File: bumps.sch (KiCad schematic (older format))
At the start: 136 parts, among them M1 CONN_1, M2 CONN_1, M3 CONN_1, P1 DIL6, P10 Mot-A, P11 Mot-A, P12 Mot-X, P13 T1, P14 T2, P15 T3, P16 MPower, P17 PWM-2, P18 PWM-1, P19 END-X, P2 DIL6, P20 END-Y, P21 END-Z, P22 Mot-X, P23 Mot-Y, P24 Mot-Y, P25 Mot-Z, P26 Mot-Z, P27 Aux, P29 PWM, P3 Mot-E, P4 Mot-E, P5 DIL6, P6 DIL6, P7 DIL6, P8 P8 Header, P9 P9 Header, Q1 IRLB8743PBF, Q2 IRLB8743PBF, Q3 FDS9926A, Q4 FDS9926A, U1 E-Polo, U2 A-Polo, U3 X-Polo, U4 Y-Polo, U5 Z-Polo, U6 MC34063, U7 AP1117/3.3

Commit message: o Fix components, that disappeared in the kicad library   (CONN_1, CONN_2 and CONN_4 don't exist anymore,   they are now CONN_01X01, CONN_01X02 and CONN_01x04). o Connect the new components that inconveniently have a different   shape, so don't connect to the original pins anymore. o My statement regarding this non-backward compatible library   change: "&%@3$%*!@"  :)
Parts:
- M1, M2, M3: symbol CONN_1 -> CONN_01X01
- P10, P11, P12, P22, P23, P24, P25, P26, P3, P4: symbol CONN_4 -> CONN_01X04
- P13, P14, P15, P16, P17, P18, P19, P20, P21, P27, P29: symbol CONN_2 -> CONN_01X02
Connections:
- wire segments 237 -> 263

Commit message: o Get rid of 100k pull-down for MS1. Not needed   (fixes #9)
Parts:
- removed R1, R2, R3, R4, R5: 100k, SMD_Packages:SM0805, symbol R
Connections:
- wire segments 263 -> 258
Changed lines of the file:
@@
 LIBS:valves
 LIBS:BUMPS
-LIBS:bumps-cache
 EELAYER 25 0
 EELAYER END
@@
 ~EN
 $Comp
-L R R1
-U 1 1 52EDAB15
-P 3700 4650
-F 0 "R1" V 3780 4650 40  0000 C CNN
-F 1 "100k" V 3707 4651 40  0000 C CNN
-F 2 "SMD_Packages:SM0805" V 3630 4650 30  0001 C CNN
-F 3 "" H 3700 4650 60  0001 C CNN
-	1    3700 4650
-	-1   0    0    1
-$EndComp
-$Comp
-L GND #PWR07
-U 1 1 52EDABD4
-P 3700 4900
-F 0 "#PWR07" H 3700 4900 30  0001 C CNN
-F 1 "GND" H 3700 4830 30  0001 C CNN
-F 2 "" H 3700 4900 60  0001 C CNN
-F 3 "" H 3700 4900 60  0001 C CNN
-	1    3700 4900
-	1    0    0    -1
-$EndComp
-$Comp
 L POLOLUSTEPPER U5
 U 1 1 52EDACE9
@@
 VDD_3V3
 $Comp
-L R R5
-U 1 1 52EDAD11
-P 7850 5050
-F 0 "R5" V 7930 5050 40  0000 C CNN
-F 1 "100k" V 7857 5051 40  0000 C CNN
-F 2 "SMD_Packages:SM0805" V 7780 5050 30  0001 C CNN
-F 3 "" H 7850 5050 60  0001 C CNN
-	1    7850 5050
-	-1   0    0    1
-$EndComp
-$Comp
-L GND #PWR010
-U 1 1 52EDAD22
-P 7850 5300
-F 0 "#PWR010" H 7850 5300 30  0001 C CNN
-F 1 "GND" H 7850 5230 30  0001 C CNN
-F 2 "" H 7850 5300 60  0001 C CNN
-F 3 "" H 7850 5300 60  0001 C CNN
-	1    7850 5300
-	-1   0    0    -1
-$EndComp
-$Comp
 L POLOLUSTEPPER U3
 U 1 1 52EDAD28
@@
 VDD_3V3
 $Comp
-L R R3
-U 1 1 52EDAD50
-P 7850 1750
-F 0 "R3" V 7930 1750 40  0000 C CNN
-F 1 "100k" V 7857 1751 40  0000 C CNN
-F 2 "SMD_Packages:SM0805" V 7780 1750 30  0001 C CNN
-F 3 "" H 7850 1750 60  0001 C CNN
-	1    7850 1750
-	-1   0    0    1
-$EndComp
-$Comp
-L GND #PWR013
-U 1 1 52EDAD61
-P 7850 2000
-F 0 "#PWR013" H 7850 2000 30  0001 C CNN
-F 1 "GND" H 7850 1930 30  0001 C CNN
-F 2 "" H 7850 2000 60  0001 C CNN
-F 3 "" H 7850 2000 60  0001 C CNN
-	1    7850 2000
-	1    0    0    -1
-$EndComp
-$Comp
 L POLOLUSTEPPER U4
 U 1 1 52EDAD67
@@
 VDD_3V3
 $Comp
-L R R4
-U 1 1 52EDAD8F
-P 7850 3400
-F 0 "R4" V 7930 3400 40  0000 C CNN
-F 1 "100k" V 7857 3401 40  0000 C CNN
-F 2 "SMD_Packages:SM0805" V 7780 3400 30  0001 C CNN
-F 3 "" H 7850 3400 60  0001 C CNN
-	1    7850 3400
-	-1   0    0    1
-$EndComp
-$Comp
-L GND #PWR016
-U 1 1 52EDADA0
-P 7850 3650
-F 0 "#PWR016" H 7850 3650 30  0001 C CNN
-F 1 "GND" H 7850 3580 30  0001 C CNN
-F 2 "" H 7850 3650 60  0001 C CNN
-F 3 "" H 7850 3650 60  0001 C CNN
-	1    7850 3650
-	1    0    0    -1
-$EndComp
-$Comp
 L POLOLUSTEPPER U2
 U 1 1 52EDADA6
@@
 Text GLabel 3100 5600 1    50   Input ~ 0
 VDD_3V3
-$Comp
-L R R2
-U 1 1 52EDADCE
-P 3700 6400
-F 0 "R2" V 3780 6400 40  0000 C CNN
-F 1 "100k" V 3707 6401 40  0000 C CNN
-F 2 "SMD_Packages:SM0805" V 3630 6400 30  0001 C CNN
-F 3 "" H 3700 6400 60  0001 C CNN
-	1    3700 6400
-	-1   0    0    1
-$EndComp
-$Comp
-L GND #PWR019
-U 1 1 52EDADDF
-P 3700 6650
-F 0 "#PWR019" H 3700 6650 30  0001 C CNN
-F 1 "GND" H 3700 6580 30  0001 C CNN
-F 2 "" H 3700 6650 60  0001 C CNN
-F 3 "" H 3700 6650 60  0001 C CNN
-	1    3700 6650
-	1    0    0    -1
-$EndComp
 Text GLabel 4100 1750 2    50   Output ~ 0
 STEP_X
@@
 	3900 4250 4300 4250
 Wire Wire Line
-	3700 4400 4050 4050
-Connection ~ 4050 4050
-Wire Wire Line
 	9950 5050 9950 5100
 Wire Wire Line
@@
 	8050 4650 8450 4650
 Wire Wire Line
-	7850 4800 8200 4450
-Connection ~ 8200 4450
-Wire Wire Line
 	9950 1750 9950 1800
 Wire Wire Line
@@
 	8050 1350 8450 1350
 Wire Wire Line
-	7850 1500 8200 1150
-Connection ~ 8200 1150
-Wire Wire Line
 	9950 3400 9950 3450
 Wire Wire Line
@@
 	8050 3000 8450 3000
 Wire Wire Line
-	7850 3150 8200 2800
-Connection ~ 8200 2800
-Wire Wire Line
 	5800 6400 5800 6450
 Wire Wire Line
@@
 Wire Wire Line
 	3900 6000 4300 6000
-Wire Wire Line
-	3700 6150 4050 5800
-Connection ~ 4050 5800
 Text GLabel 5100 1350 0    50   Input ~ 0
 END_X

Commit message: o Use 10uF ceramic capacitors in analog section. Makes that part more   compact and nicer to assemble.   Fixes #7
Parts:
- C10, C11, C14, C9: footprint Capacitors_SMD:c_elec_4x5.7 -> Capacitors_SMD:C_0805; symbol CAPAPOL -> C

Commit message: o Add 4k7 pullup to ~Enable o Version number on board-text bumped to v0.2 o Addresses 'enable' part of issue #4
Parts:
- added R1: 4k7, Resistors_SMD:R_0805, symbol R
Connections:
- wire segments 258 -> 260
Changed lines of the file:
@@
 Text GLabel 3200 3850 1    50   Input ~ 0
 VDD_3V3
-Text GLabel 4100 1250 2    50   Output ~ 0
+Text GLabel 4550 1250 2    50   Output ~ 0
 ~EN
 $Comp
@@
 F 0 "Q3" H 1500 6951 40  0000 R CNN
 F 1 "FDS9926A" H 1500 7250 40  0000 R CNN
-F 2 "SOIC_Packages:SOIC-8_N" H 1370 7202 25  0000 C CIN
+F 2 "SOIC_Packages:SOIC-8_N" H 1370 7202 25  0001 C CIN
 F 3 "" H 1500 7100 60  0000 C CNN
 	1    1500 7100
@@
 F 0 "Q3" H 1500 7801 40  0000 R CNN
 F 1 "FDS9926A" H 1500 8100 40  0000 R CNN
-F 2 "SOIC_Packages:SOIC-8_N" H 1370 8052 25  0000 C CIN
+F 2 "SOIC_Packages:SOIC-8_N" H 1370 8052 25  0001 C CIN
 F 3 "" H 1500 7950 60  0000 C CNN
 	2    1500 7950
@@
 F 0 "Q4" H 1550 5451 40  0000 R CNN
 F 1 "FDS9926A" H 1550 5750 40  0000 R CNN
-F 2 "SOIC_Packages:SOIC-8_N" H 1420 5702 25  0000 C CIN
+F 2 "SOIC_Packages:SOIC-8_N" H 1420 5702 25  0001 C CIN
 F 3 "" H 1550 5600 60  0000 C CNN
 	1    1550 5600
@@
 F 0 "Q4" H 1550 6051 40  0000 R CNN
 F 1 "FDS9926A" H 1550 6350 40  0000 R CNN
-F 2 "SOIC_Packages:SOIC-8_N" H 1420 6302 25  0000 C CIN
+F 2 "SOIC_Packages:SOIC-8_N" H 1420 6302 25  0001 C CIN
 F 3 "" H 1550 6200 60  0000 C CNN
 	2    1550 6200
@@
 Wire Wire Line
 	10200 6800 10200 6850
+$Comp
+L R R1
+U 1 1 5570C85C
+P 4500 1000
+F 0 "R1" V 4400 1000 40  0000 C CNN
+F 1 "4k7" V 4507 1001 40  0000 C CNN
+F 2 "Resistors_SMD:R_0805" V 4430 1000 30  0001 C CNN
+F 3 "" H 4500 1000 30  0000 C CNN
+	1    4500 1000
+	1    0    0    1
+$EndComp
+Text GLabel 4500 650  2    50   Input ~ 0
+VDD_3V3
+Wire Wire Line
+	4100 1250 4550 1250
+Connection ~ 4500 1250
+Wire Wire Line
+	4500 650  4500 750
 $EndSCHEMATC

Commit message: o Change footprint of power-FET to have the heat-sink on the right side. o Addresses part of issue #4
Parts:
- Q1, Q2: footprint Transistors_TO-220:TO-220_FET-GDS_Vertical_MountedFromLS -> Transistors_TO-220:TO-220_FET-GDS_Vertical_LargePads
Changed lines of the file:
@@
 F 0 "Q2" H 1760 4820 60  0000 R CNN
 F 1 "IRLB8743PBF" H 1600 4750 60  0000 R CNN
-F 2 "Transistors_TO-220:TO-220_FET-GDS_Vertical_MountedFromLS" H 1750 4650 60  0001 C CNN
+F 2 "Transistors_TO-220:TO-220_FET-GDS_Vertical_LargePads" H 1750 4650 60  0001 C CNN
 F 3 "" H 1750 4650 60  0000 C CNN
 	1    1750 4650
@@
 F 0 "Q1" H 1760 4020 60  0000 R CNN
 F 1 "IRLB8743PBF" H 1600 3950 60  0000 R CNN
-F 2 "Transistors_TO-220:TO-220_FET-GDS_Vertical_MountedFromLS" H 1750 3850 60  0001 C CNN
+F 2 "Transistors_TO-220:TO-220_FET-GDS_Vertical_LargePads" H 1750 3850 60  0001 C CNN
 F 3 "" H 1750 3850 60  0000 C CNN
 	1    1750 3850

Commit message: o Rename motor labels from 'Polo X' to 'Motor 1'. The axis assignment   is not done in the hardware, but can be freely assigned in the   software. So this would be confusing.
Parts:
- U1: value E-Polo -> Motor-2
- U2: value A-Polo -> Motor-4
- U3: value X-Polo -> Motor-5
- U4: value Y-Polo -> Motor-3
- U5: value Z-Polo -> Motor-1
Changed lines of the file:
@@
 P 5050 4300
 F 0 "U1" H 5050 4300 50  0000 C CNN
-F 1 "E-Polo" H 5050 4800 50  0000 C CNN
+F 1 "Motor-2" H 5050 4800 50  0000 C CNN
 F 2 "bumps:POLOLU" H 5100 4700 50  0001 C CNN
 F 3 "DOCUMENTATION" H 5050 3800 50  0001 C CNN
@@
 P 9200 4700
 F 0 "U5" H 9200 4700 50  0000 C CNN
-F 1 "Z-Polo" H 9200 5200 50  0000 C CNN
+F 1 "Motor-1" H 9200 5200 50  0000 C CNN
 F 2 "bumps:POLOLU" H 9250 5100 50  0001 C CNN
 F 3 "DOCUMENTATION" H 9200 4200 50  0001 C CNN
@@
 P 9200 1400
 F 0 "U3" H 9200 1400 50  0000 C CNN
-F 1 "X-Polo" H 9200 1900 50  0000 C CNN
+F 1 "Motor-5" H 9200 1900 50  0000 C CNN
 F 2 "bumps:POLOLU" H 9250 1800 50  0001 C CNN
 F 3 "DOCUMENTATION" H 9200 900 50  0001 C CNN
@@
 P 9200 3050
 F 0 "U4" H 9200 3050 50  0000 C CNN
-F 1 "Y-Polo" H 9200 3550 50  0000 C CNN
+F 1 "Motor-3" H 9200 3550 50  0000 C CNN
 F 2 "bumps:POLOLU" H 9250 3450 50  0001 C CNN
 F 3 "DOCUMENTATION" H 9200 2550 50  0001 C CNN
@@
 P 5050 6050
 F 0 "U2" H 5050 6050 50  0000 C CNN
-F 1 "A-Polo" H 5050 6550 50  0000 C CNN
+F 1 "Motor-4" H 5050 6550 50  0000 C CNN
 F 2 "bumps:POLOLU" H 5100 6450 50  0001 C CNN
 F 3 "DOCUMENTATION" H 5050 5550 50  0001 C CNN

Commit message: o little re-arrange stuff and add start of EStop input.
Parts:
- removed C18, C19: 100n, SMD_Packages:SM0805, symbol C
- added P28: K1, Connect:PINTST, symbol CONN_01X01
- added P30: K2, Connect:PINTST, symbol CONN_01X01
- added R2: 330, SMD_Packages:SM0805, symbol R
- added R3: 4k7, SMD_Packages:SM0805, symbol R
- added U8: OPTO-TRANSISTOR4, Opto-Devices:Optocoupler_SMD_HandSoldering_KPC357_LTV35x_PC357_SingleChannel, symbol OPTO-TRANSISTOR4
- C10, C11, C14, C9: footprint Capacitors_SMD:C_0805 -> Capacitors_SMD:c_elec_4x5.7
- Q1, Q2: footprint Transistors_TO-220:TO-220_FET-GDS_Vertical_LargePads -> Transistors_TO-220:TO-220_FET-GDS_Vertical_MountedFromLS
- R1: footprint Resistors_SMD:R_0805 -> SMD_Packages:SM0805
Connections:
- net labels added: ~EStop
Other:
- note added: "Normal case: LED on, ~EStop~ pulled to High."
- note added: "Switch NC"
- note removed: "capacitors on LED-resistors to\naccentuate voltage transients"
- moved on the sheet: C13, C14, C15, C16, C17, C20, C21, C22, C23, C24, C6, D24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

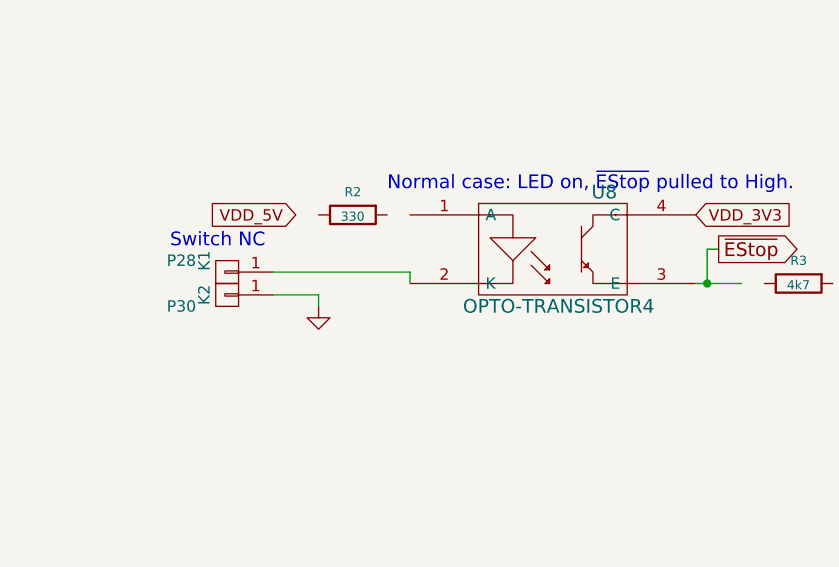
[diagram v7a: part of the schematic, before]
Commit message: o convert library to .pretty o add DIL-4 for OptoCoupler (Didn't find it in lib?) and 0.2" distance   Wide header for the Estop switch. o assignement and import into pcb, but not routed yet. o make a bit more space to add another end-switch (the visual glitch detector   capacitors on the LEDs had to go).
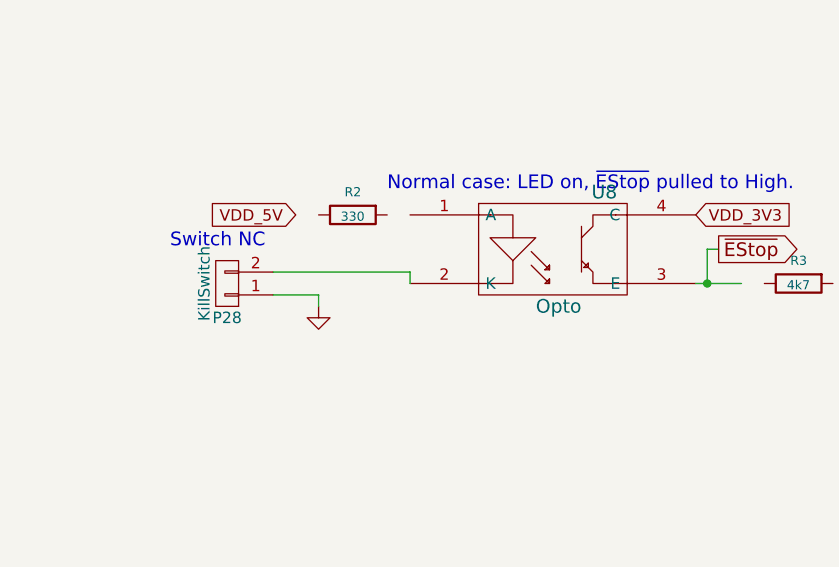
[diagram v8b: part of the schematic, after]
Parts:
- removed P28: K1, Connect:PINTST, symbol CONN_01X01
- removed P30: K2, Connect:PINTST, symbol CONN_01X01
- added P28: KillSwitch, bumps:WideHeader, symbol CONN_01X02
- C10, C11, C14, C9: footprint Capacitors_SMD:c_elec_4x5.7 -> Capacitors_SMD:C_0805
- Q1, Q2: footprint Transistors_TO-220:TO-220_FET-GDS_Vertical_MountedFromLS -> Transistors_TO-220:TO-220_FET-GDS_Vertical_LargePads
- R1: footprint SMD_Packages:SM0805 -> Resistors_SMD:R_0805
- U8: value OPTO-TRANSISTOR4 -> Opto; footprint Opto-Devices:Optocoupler_SMD_HandSoldering_KPC357_LTV35x_PC357_SingleChannel -> bumps:DIL-4
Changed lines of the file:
@@
 F 0 "Q2" H 1760 4820 60  0000 R CNN
 F 1 "IRLB8743PBF" H 1600 4750 60  0000 R CNN
-F 2 "Transistors_TO-220:TO-220_FET-GDS_Vertical_MountedFromLS" H 1750 4650 60  0001 C CNN
+F 2 "Transistors_TO-220:TO-220_FET-GDS_Vertical_LargePads" H 1750 4650 60  0001 C CNN
 F 3 "" H 1750 4650 60  0000 C CNN
 	1    1750 4650
@@
 F 0 "Q1" H 1760 4020 60  0000 R CNN
 F 1 "IRLB8743PBF" H 1600 3950 60  0000 R CNN
-F 2 "Transistors_TO-220:TO-220_FET-GDS_Vertical_MountedFromLS" H 1750 3850 60  0001 C CNN
+F 2 "Transistors_TO-220:TO-220_FET-GDS_Vertical_LargePads" H 1750 3850 60  0001 C CNN
 F 3 "" H 1750 3850 60  0000 C CNN
 	1    1750 3850
@@
 F 0 "C10" H 1250 2150 40  0000 L CNN
 F 1 "10u" H 1250 1950 40  0000 L CNN
-F 2 "Capacitors_SMD:c_elec_4x5.7" H 1300 1900 30  0001 C CNN
+F 2 "Capacitors_SMD:C_0805" H 1300 1900 30  0001 C CNN
 F 3 "" H 1200 2050 300 0000 C CNN
 	1    1200 2050
@@
 F 0 "C14" H 6650 9000 40  0000 L CNN
 F 1 "10u" H 6650 8800 40  0000 L CNN
-F 2 "Capacitors_SMD:c_elec_4x5.7" H 6700 8750 30  0001 C CNN
+F 2 "Capacitors_SMD:C_0805" H 6700 8750 30  0001 C CNN
 F 3 "" H 6600 8900 300 0000 C CNN
 	1    6600 8900
@@
 F 0 "C9" H 1250 1250 40  0000 L CNN
 F 1 "10u" H 1250 1050 40  0000 L CNN
-F 2 "Capacitors_SMD:c_elec_4x5.7" H 1300 1000 30  0001 C CNN
+F 2 "Capacitors_SMD:C_0805" H 1300 1000 30  0001 C CNN
 F 3 "" H 1200 1150 300 0000 C CNN
 	1    1200 1150
@@
 F 0 "C11" H 1250 3050 40  0000 L CNN
 F 1 "10u" H 1250 2850 40  0000 L CNN
-F 2 "Capacitors_SMD:c_elec_4x5.7" H 1300 2800 30  0001 C CNN
+F 2 "Capacitors_SMD:C_0805" H 1300 2800 30  0001 C CNN
 F 3 "" H 1200 2950 300 0000 C CNN
 	1    1200 2950
@@
 F 0 "R1" V 4400 1000 40  0000 C CNN
 F 1 "4k7" V 4507 1001 40  0000 C CNN
-F 2 "SMD_Packages:SM0805" V 4430 1000 30  0001 C CNN
+F 2 "Resistors_SMD:R_0805" V 4430 1000 30  0001 C CNN
 F 3 "" H 4500 1000 30  0000 C CNN
 	1    4500 1000
@@
 P 9550 8000
 F 0 "U8" H 9750 8250 60  0000 C CNN
-F 1 "OPTO-TRANSISTOR4" H 9550 7750 60  0000 C CNN
-F 2 "Opto-Devices:Optocoupler_SMD_HandSoldering_KPC357_LTV35x_PC357_SingleChannel" H 9550 8000 60  0001 C CNN
+F 1 "Opto" H 9550 7750 60  0000 C CNN
+F 2 "bumps:DIL-4" H 9550 8000 60  0001 C CNN
 F 3 "" H 9550 8000 60  0000 C CNN
 	1    9550 8000
@@
 	8500 8200 8500 8250
 $Comp
-L CONN_01X01 P28
-U 1 1 5577CD3E
-P 8100 8100
-F 0 "P28" H 8300 8050 50  0000 C CNN
-F 1 "K1" V 8200 8050 50  0000 C CNN
-F 2 "Connect:PINTST" H 8100 8100 60  0001 C CNN
-F 3 "" H 8100 8100 60  0000 C CNN
-	1    8100 8100
+L CONN_01X02 P28
+U 1 1 557008FF
+P 8100 8150
+F 0 "P28" H 8100 8300 50  0000 C CNN
+F 1 "KillSwitch" V 8200 8150 50  0000 C CNN
+F 2 "bumps:WideHeader" H 8100 8150 60  0001 C CNN
+F 3 "" H 8100 8150 60  0000 C CNN
+	1    8100 8150
 	-1   0    0    1
 $EndComp
-$Comp
-L CONN_01X01 P30
-U 1 1 5577CDE7
-P 8100 8200
-F 0 "P30" H 8300 8250 50  0000 C CNN
-F 1 "K2" V 8200 8200 50  0000 C CNN
-F 2 "Connect:PINTST" H 8100 8200 60  0001 C CNN
-F 3 "" H 8100 8200 60  0000 C CNN
-	1    8100 8200
-	-1   0    0    1
-$EndComp
